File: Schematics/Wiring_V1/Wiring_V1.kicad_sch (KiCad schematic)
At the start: 4 parts, among them Q1 IRFZ44N

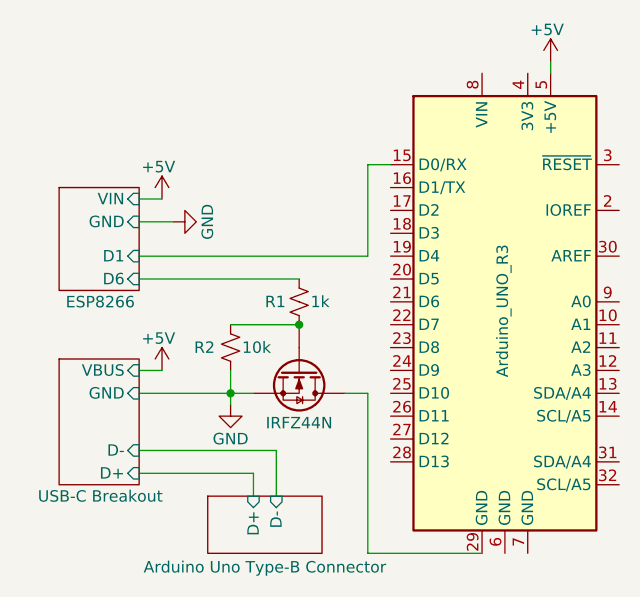
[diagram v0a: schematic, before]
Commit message: Updated wiring schematic
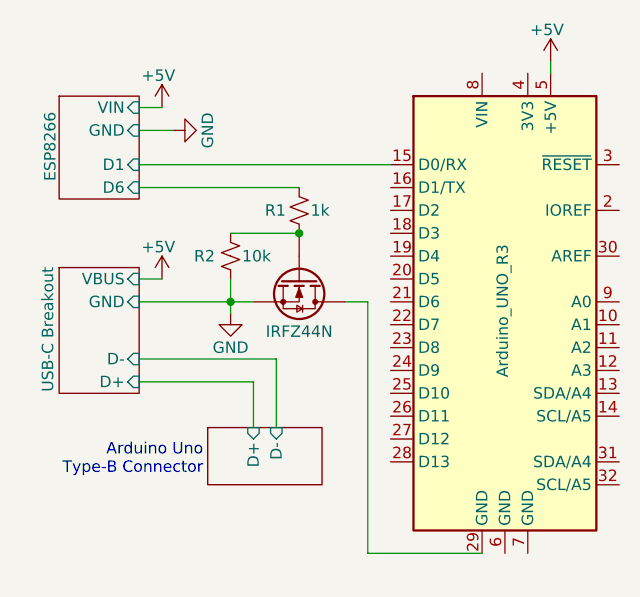
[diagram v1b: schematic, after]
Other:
- note added: "Arduino Uno Type-B Connector"
- moved on the sheet: R1, R2
